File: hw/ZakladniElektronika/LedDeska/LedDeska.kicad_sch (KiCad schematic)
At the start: 13 parts, among them U1 LDC1614

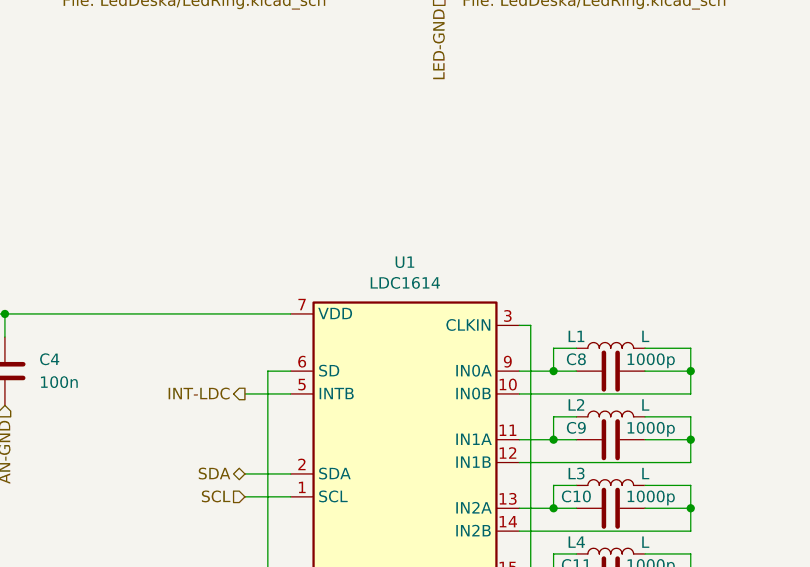
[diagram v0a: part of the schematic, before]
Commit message: Likvidace MiniUI jako samostatné desky a výběr všech komponent
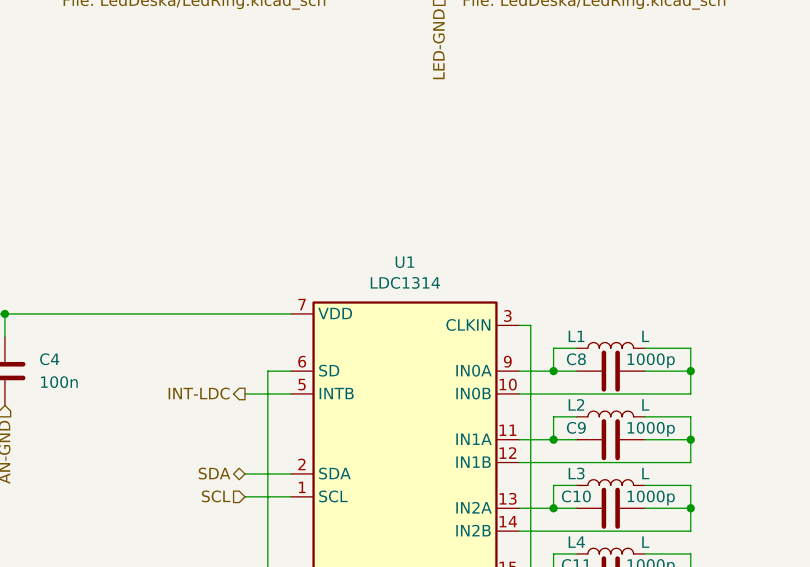
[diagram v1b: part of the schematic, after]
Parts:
- C1, C2: footprint Capacitor_SMD:C_0603_1608Metric -> Capacitor_SMD:C_0805_2012Metric; Basic/Extended B -> (none); LCSC C96446 -> C15850; info 25V, X5R -> (none)
- C10, C11, C8, C9: Basic/Extended B -> (none); info 50V, X7R -> (none)
- C3: JLCPCB_CORRECTION 0;0;0 -> (none); info 50V, X5R (potenciálně C52923 což je 25V, X5R ) -> 50V, X7R
- L1, L2, L3, L4: footprint RKL-Inductors:PCB_coil -> BB:coil; JLCPCB_IGNORE ignore -> (none)
- U1: value LDC1614 -> LDC1314; footprint Package_DFN_QFN:WQFN-16-1EP_4x4mm_P0.5mm_EP2.6x2.6mm -> Package_DFN_QFN:WQFN-16-1EP_4x4mm_P0.5mm_EP2.6x2.6mm_ThermalVias; Basic/Extended E -> (none); LCSC C968448 -> C80399
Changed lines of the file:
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@@
       (effects (font (size 1.27 1.27)))
     )
-    (property "Footprint" "RKL-Inductors:PCB_coil" (at 181.61 105.41 0)
+    (property "Footprint" "BB:coil" (at 181.61 105.41 0)
       (effects (font (size 1.27 1.27)) hide)
     )
     (property "Datasheet" "~" (at 181.61 105.41 0)
-      (effects (font (size 1.27 1.27)) hide)
-    )
-    (property "JLCPCB_IGNORE" "ignore" (at 181.61 105.41 0)
       (effects (font (size 1.27 1.27)) hide)
     )
@@
       (effects (font (size 1.27 1.27)) hide)
     )
-    (property "info" "50V, X5R (potenciálně C52923 což je 25V, X5R )" (at 101.6 107.95 0)
+    (property "info" "50V, X7R" (at 101.6 107.95 0)
       (effects (font (size 1.27 1.27)) hide)
     )
@@
       (effects (font (size 1.27 1.27)) hide)
     )
-    (property "JLCPCB_CORRECTION" "0;0;0" (at 101.6 107.95 0)
-      (effects (font (size 1.27 1.27)) hide)
-    )
     (pin "1")
     (pin "2")
@@
       (effects (font (size 1.27 1.27)) hide)
     )
-    (property "Basic/Extended" "B" (at 181.61 107.95 0)
-      (effects (font (size 1.27 1.27)) hide)
-    )
-    (property "info" "50V, X7R" (at 181.61 107.95 0)
-      (effects (font (size 1.27 1.27)) hide)
-    )
     (pin "1")
     (pin "2")
@@
       (effects (font (size 1.27 1.27)) hide)
     )
-    (property "Basic/Extended" "B" (at 181.61 115.57 0)
-      (effects (font (size 1.27 1.27)) hide)
-    )
-    (property "info" "50V, X7R" (at 181.61 115.57 0)
-      (effects (font (size 1.27 1.27)) hide)
-    )
     (pin "1")
     (pin "2")
@@
       (effects (font (size 1.27 1.27)) hide)
     )
-    (property "Basic/Extended" "B" (at 181.61 130.81 0)
-      (effects (font (size 1.27 1.27)) hide)
-    )
-    (property "info" "50V, X7R" (at 181.61 130.81 0)
-      (effects (font (size 1.27 1.27)) hide)
-    )
     (pin "1")
     (pin "2")
@@
       (effects (font (size 1.27 1.27)))
     )
-    (property "Value" "LDC1614" (at 158.75 98.1964 0)
-      (effects (font (size 1.27 1.27)))
-    )
-    (property "Footprint" "Package_DFN_QFN:WQFN-16-1EP_4x4mm_P0.5mm_EP2.6x2.6mm" (at 158.75 99.06 0)
+    (property "Value" "LDC1314" (at 158.75 98.1964 0)
+      (effects (font (size 1.27 1.27)))
+    )
+    (property "Footprint" "Package_DFN_QFN:WQFN-16-1EP_4x4mm_P0.5mm_EP2.6x2.6mm_ThermalVias" (at 158.75 99.06 0)
       (effects (font (size 1.27 1.27)) hide)
     )
@@
       (effects (font (size 1.27 1.27)) hide)
     )
-    (property "LCSC" "C968448" (at 158.75 118.11 0)
-      (effects (font (size 1.27 1.27)) hide)
-    )
-    (property "Basic/Extended" "E" (at 158.75 118.11 0)
+    (property "LCSC" "C80399" (at 158.75 118.11 0)
       (effects (font (size 1.27 1.27)) hide)
     )
@@
       (effects (font (size 1.27 1.27)))
     )
-    (property "Footprint" "RKL-Inductors:PCB_coil" (at 181.61 120.65 0)
+    (property "Footprint" "BB:coil" (at 181.61 120.65 0)
       (effects (font (size 1.27 1.27)) hide)
     )
@@
       (effects (font (size 1.27 1.27)) hide)
     )
-    (property "JLCPCB_IGNORE" "ignore" (at 181.61 120.65 0)
-      (effects (font (size 1.27 1.27)) hide)
-    )
     (pin "1")
     (pin "2")
@@
       (effects (font (size 1.27 1.27)))
     )
-    (property "Footprint" "RKL-Inductors:PCB_coil" (at 181.61 128.27 0)
+    (property "Footprint" "BB:coil" (at 181.61 128.27 0)
       (effects (font (size 1.27 1.27)) hide)
     )
@@
       (effects (font (size 1.27 1.27)) hide)
     )
-    (property "JLCPCB_IGNORE" "ignore" (at 181.61 128.27 0)
-      (effects (font (size 1.27 1.27)) hide)
-    )
     (pin "1")
     (pin "2")
@@
       (effects (font (size 1.27 1.27)))
     )
-    (property "Footprint" "RKL-Inductors:PCB_coil" (at 181.61 113.03 0)
+    (property "Footprint" "BB:coil" (at 181.61 113.03 0)
       (effects (font (size 1.27 1.27)) hide)
     )
     (property "Datasheet" "~" (at 181.61 113.03 0)
-      (effects (font (size 1.27 1.27)) hide)
-    )
-    (property "JLCPCB_IGNORE" "ignore" (at 181.61 113.03 0)
       (effects (font (size 1.27 1.27)) hide)
     )
@@
       (effects (font (size 1.27 1.27)) (justify left))
     )
-    (property "Footprint" "Capacitor_SMD:C_0603_1608Metric" (at 92.4052 60.96 0)
+    (property "Footprint" "Capacitor_SMD:C_0805_2012Metric" (at 92.4052 60.96 0)
       (effects (font (size 1.27 1.27)) hide)
     )
@@
       (effects (font (size 1.27 1.27)) hide)
     )
-    (property "LCSC" "C96446" (at 91.44 57.15 0)
-      (effects (font (size 1.27 1.27)) hide)
-    )
-    (property "Basic/Extended" "B" (at 91.44 57.15 0)
-      (effects (font (size 1.27 1.27)) hide)
-    )
-    (property "info" "25V, X5R" (at 91.44 57.15 0)
+    (property "LCSC" "C15850" (at 91.44 57.15 0)
       (effects (font (size 1.27 1.27)) hide)
     )
@@
     )
     (property "LCSC" "C1523" (at 181.61 123.19 90)
-      (effects (font (size 1.27 1.27)) hide)
-    )
-    (property "Basic/Extended" "B" (at 181.61 123.19 0)
-      (effects (font (size 1.27 1.27)) hide)
-    )
-    (property "info" "50V, X7R" (at 181.61 123.19 0)
       (effects (font (size 1.27 1.27)) hide)
     )
@@
       (effects (font (size 1.27 1.27)) (justify left))
     )
-    (property "Footprint" "Capacitor_SMD:C_0603_1608Metric" (at 82.2452 60.96 0)
+    (property "Footprint" "Capacitor_SMD:C_0805_2012Metric" (at 82.2452 60.96 0)
       (effects (font (size 1.27 1.27)) hide)
     )
@@
       (effects (font (size 1.27 1.27)) hide)
     )
-    (property "LCSC" "C96446" (at 81.28 57.15 0)
-      (effects (font (size 1.27 1.27)) hide)
-    )
-    (property "Basic/Extended" "B" (at 81.28 57.15 0)
-      (effects (font (size 1.27 1.27)) hide)
-    )
-    (property "info" "25V, X5R" (at 81.28 57.15 0)
-      (effects (font (size 1.27 1.27)) hide)
-    )
+    (property "LCSC" "C15850" (at 81.28 57.15 0)
+      (effects (font (size 1.27 1.27)) hide)
+    )
